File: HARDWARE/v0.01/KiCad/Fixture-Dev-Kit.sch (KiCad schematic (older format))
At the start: 1 part, among them J1 POWER

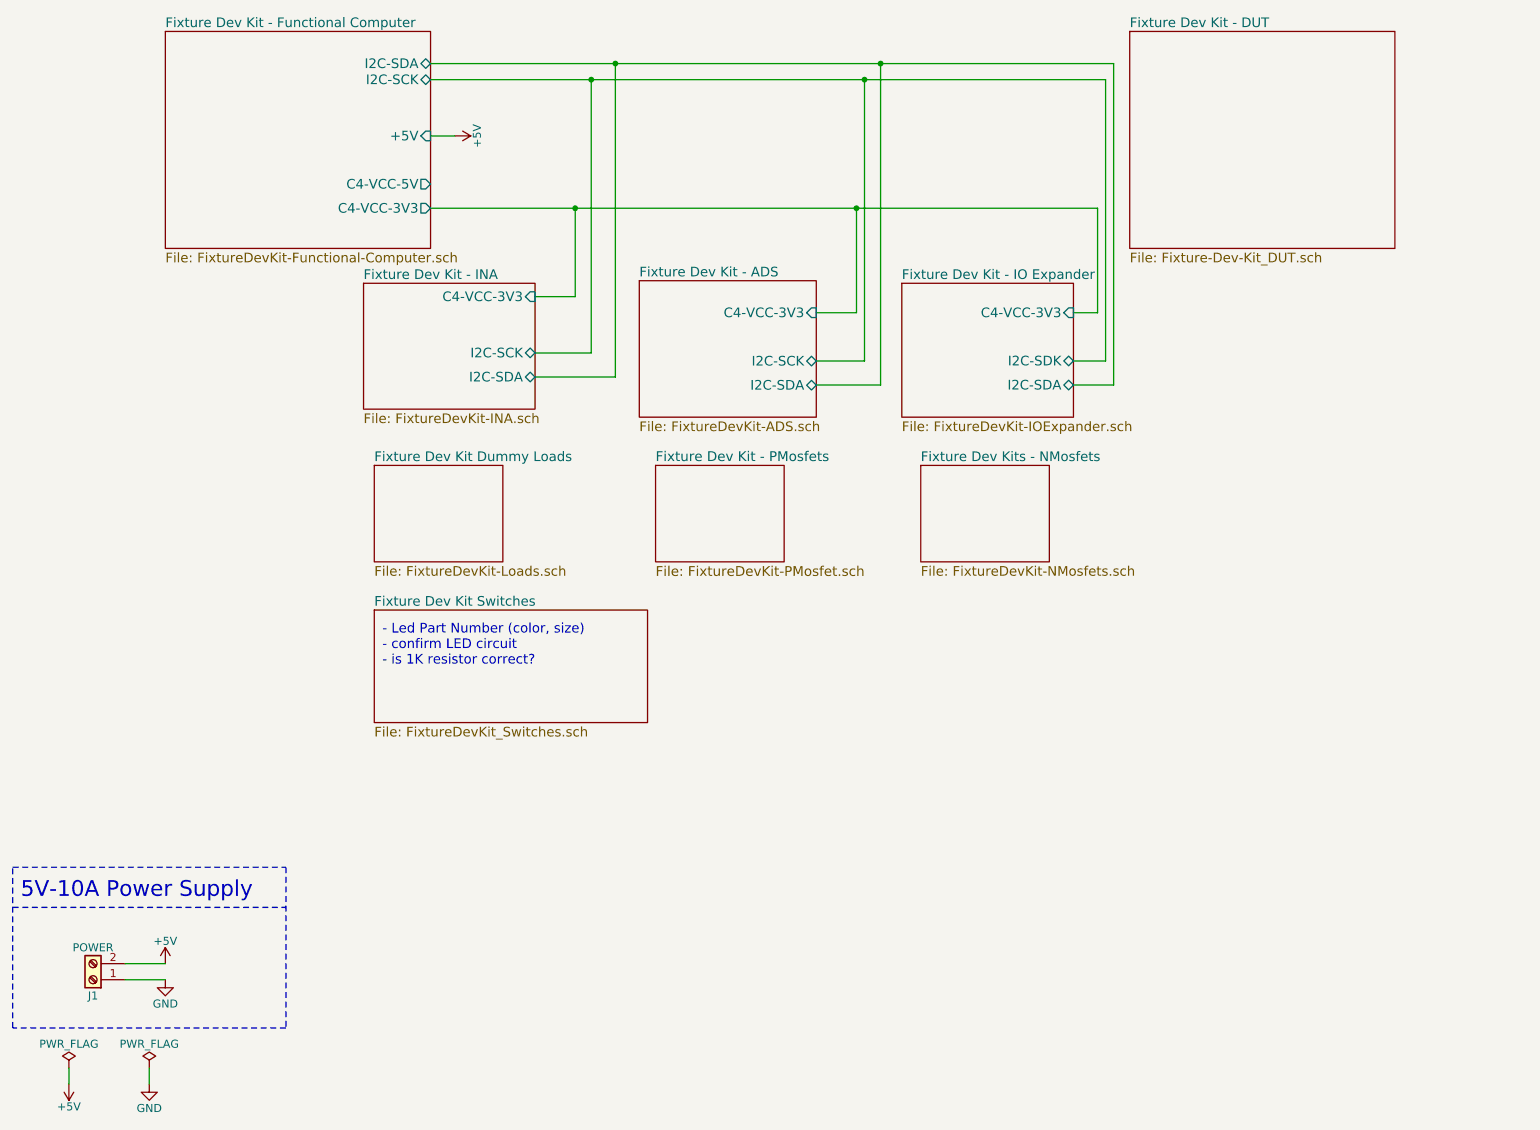
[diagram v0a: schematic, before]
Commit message: quasi-redoing entire schematic and layout
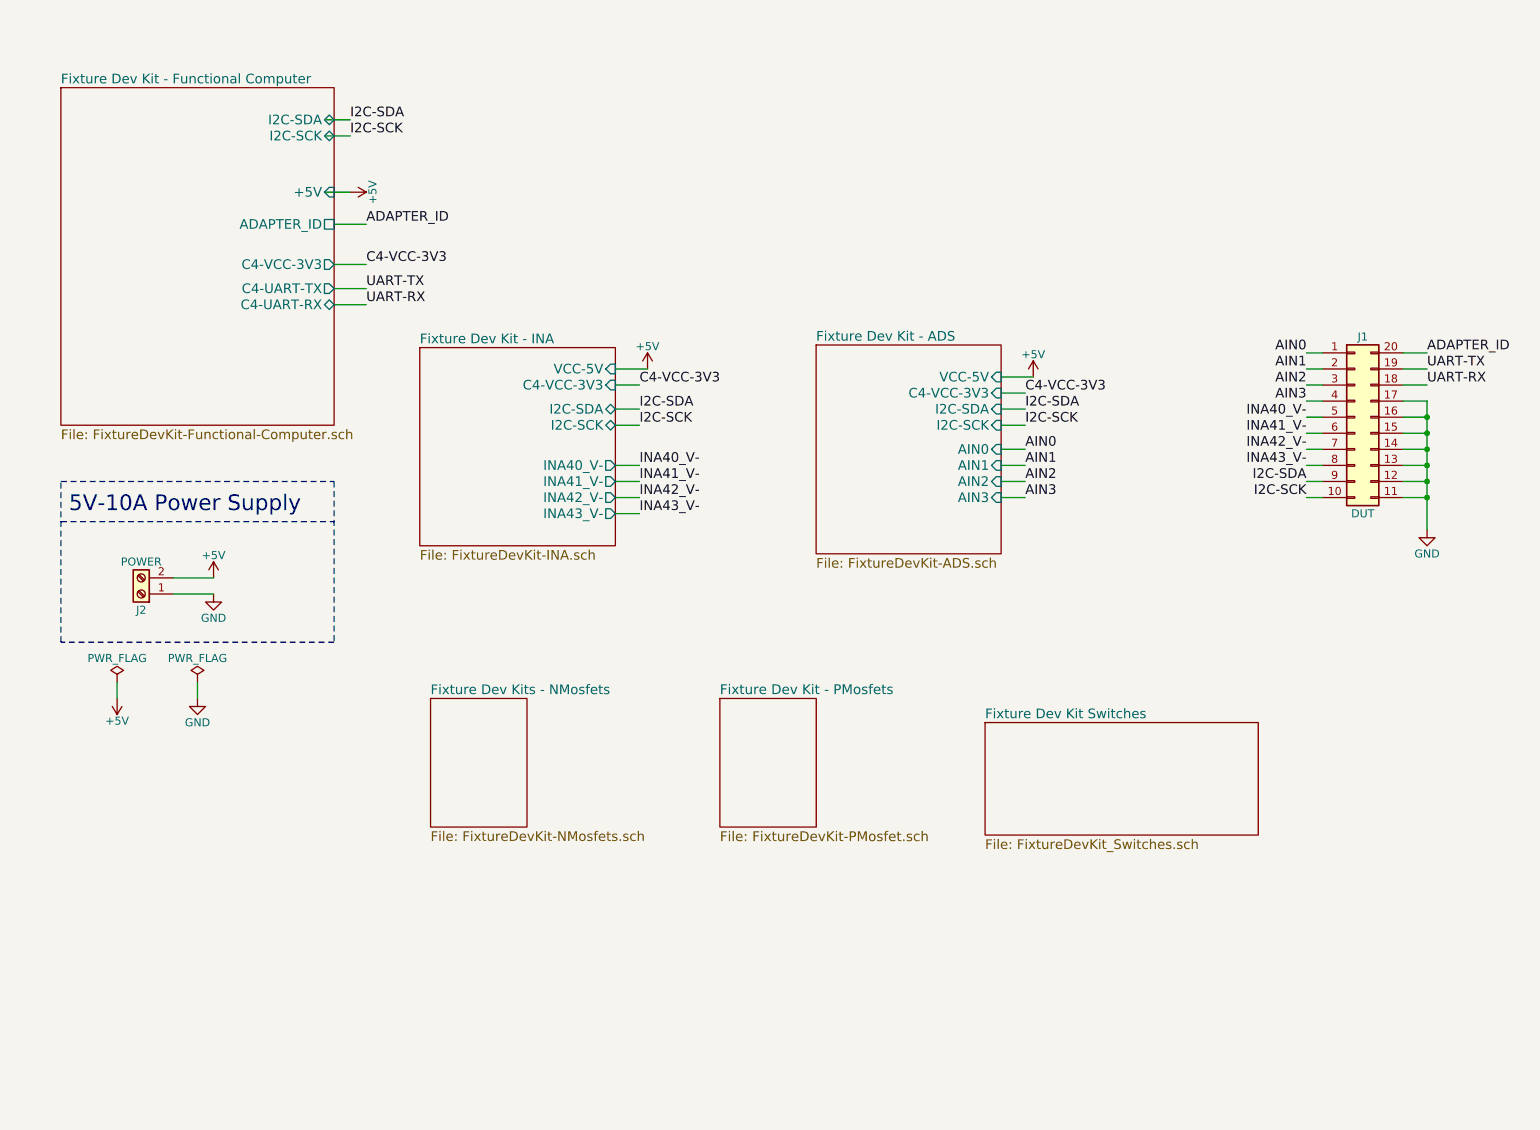
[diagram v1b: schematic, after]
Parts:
- added J1: DUT, Pin_Headers:Pin_Header_Straight_2x10_Pitch2.54mm, symbol Conn_02x10_Counter_Clockwise
- renumbered J1 to J2
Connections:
- net labels added: ADAPTER_ID, AIN0, AIN1, AIN2, AIN3, C4-VCC-3V3, I2C-SCK, I2C-SDA, INA40_V-, INA41_V-, INA42_V-, INA43_V-, UART-RX, UART-TX
- wire segments 26 -> 48
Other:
- note removed: "- Led Part Number (color, size)\n- confirm LED circuit\n- is 1K resistor correct?"
- moved on the sheet: J2

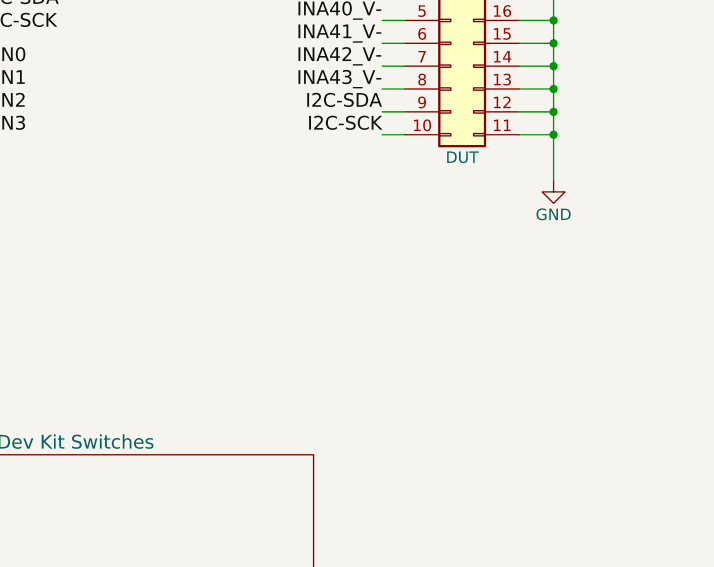
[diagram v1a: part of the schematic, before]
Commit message: updating layout footprints and board outline
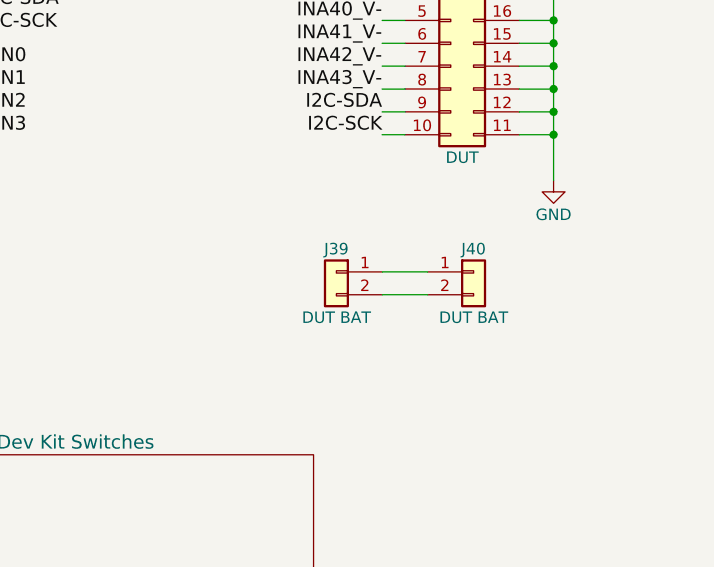
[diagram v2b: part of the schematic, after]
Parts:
- added J39: DUT BAT, Connectors_JST:JST_PH_B2B-PH-K_02x2.00mm_Straight, symbol Conn_01x02
- added J40: DUT BAT, Pin_Headers:Pin_Header_Straight_1x02_Pitch2.54mm, symbol Conn_01x02
- J2: footprint TerminalBlocks_Phoenix:TerminalBlock_Phoenix_MPT-2.54mm_2pol -> TerminalBlocks:2Pin5.08
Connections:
- wire segments 48 -> 50
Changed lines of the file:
@@
 F 0 "J2" H 1350 4550 50  0000 C CNN
 F 1 "POWER" H 1350 4250 50  0000 C CNN
-F 2 "TerminalBlocks_Phoenix:TerminalBlock_Phoenix_MPT-2.54mm_2pol" H 1350 4450 50  0001 C CNN
+F 2 "TerminalBlocks:2Pin5.08" H 1350 4450 50  0001 C CNN
 F 3 "" H 1350 4450 50  0001 C CNN
 	1    1350 4450
@@
 Wire Wire Line
 	4500 3050 4300 3050
+$Comp
+L Conn_01x02 J40
+U 1 1 59FA8B87
+P 9000 4450
+F 0 "J40" H 9000 4550 50  0000 C CNN
+F 1 "DUT BAT" H 9000 4250 50  0000 C CNN
+F 2 "Pin_Headers:Pin_Header_Straight_1x02_Pitch2.54mm" H 9000 4450 50  0001 C CNN
+F 3 "" H 9000 4450 50  0001 C CNN
+	1    9000 4450
+	1    0    0    -1
+$EndComp
+$Comp
+L Conn_01x02 J39
+U 1 1 59FA8E88
+P 8400 4450
+F 0 "J39" H 8400 4550 50  0000 C CNN
+F 1 "DUT BAT" H 8400 4250 50  0000 C CNN
+F 2 "Connectors_JST:JST_PH_B2B-PH-K_02x2.00mm_Straight" H 8400 4450 50  0001 C CNN
+F 3 "" H 8400 4450 50  0001 C CNN
+	1    8400 4450
+	-1   0    0    -1
+$EndComp
+Wire Wire Line
+	8800 4450 8600 4450
+Wire Wire Line
+	8600 4550 8800 4550
 $EndSCHEMATC
